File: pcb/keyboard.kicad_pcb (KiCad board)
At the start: 2 copper layers, 70 x 88.5 mm, 23 parts, among them SW1 SW_Push, SW2 SW_Push, SW3 RotaryEncoder_Switch, SW4 SW_Push, SW5 SW_Push, SW6 SW_Push, SW7 SW_Push, SW8 SW_Push, SW9 SW_Push, U1 MODULE-SEEEDUINO-XIAO-RP2040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

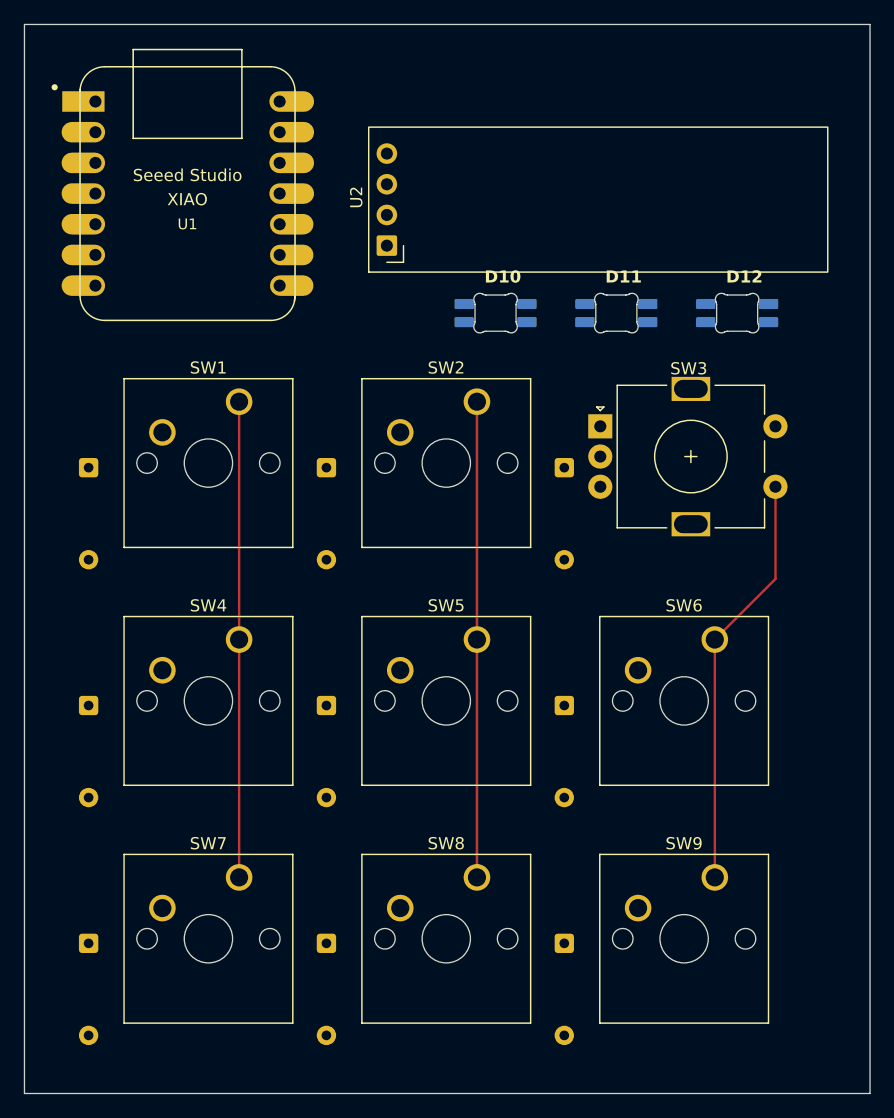
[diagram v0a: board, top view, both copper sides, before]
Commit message: align diodes in a better way
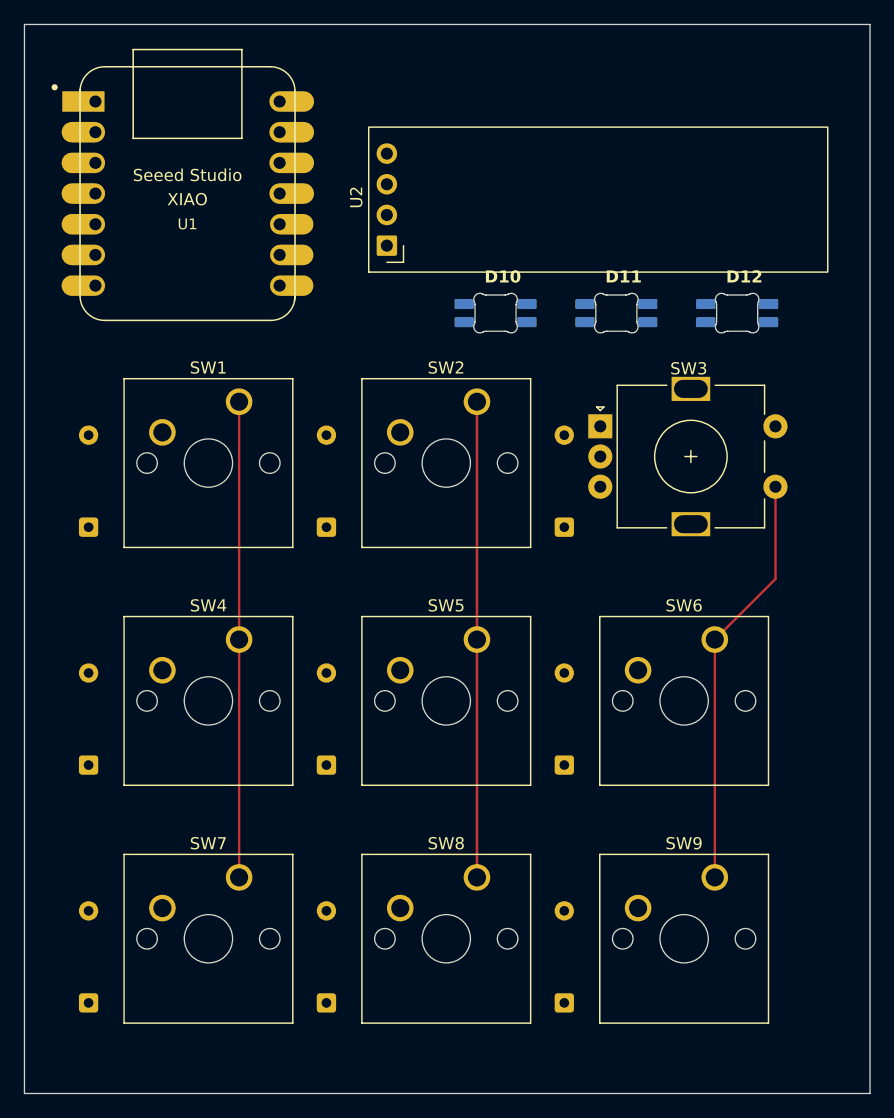
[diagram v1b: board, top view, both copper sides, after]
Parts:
- moved D1 59.3 mm to (205.2, 127.5), turned to 90 degrees
- moved D3 59.3 mm to (165.8, 127.5), turned to 90 degrees
- moved D7 52.3 mm to (205.2, 88.1), turned to 90 degrees
- moved D9 52.3 mm to (165.8, 88.1), turned to 90 degrees
- moved D2 44.3 mm to (185.5, 127.5), turned to 90 degrees
- moved D4 39.7 mm to (205.2, 107.8), turned to 90 degrees
- moved D6 39.7 mm to (165.8, 107.8), turned to 90 degrees
- moved D8 34.4 mm to (185.5, 88.1), turned to 90 degrees
- moved D5 4.93 mm to (185.5, 107.8), turned to 90 degrees

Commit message: align diodes correctly and connect them to the switches and in rows/columns
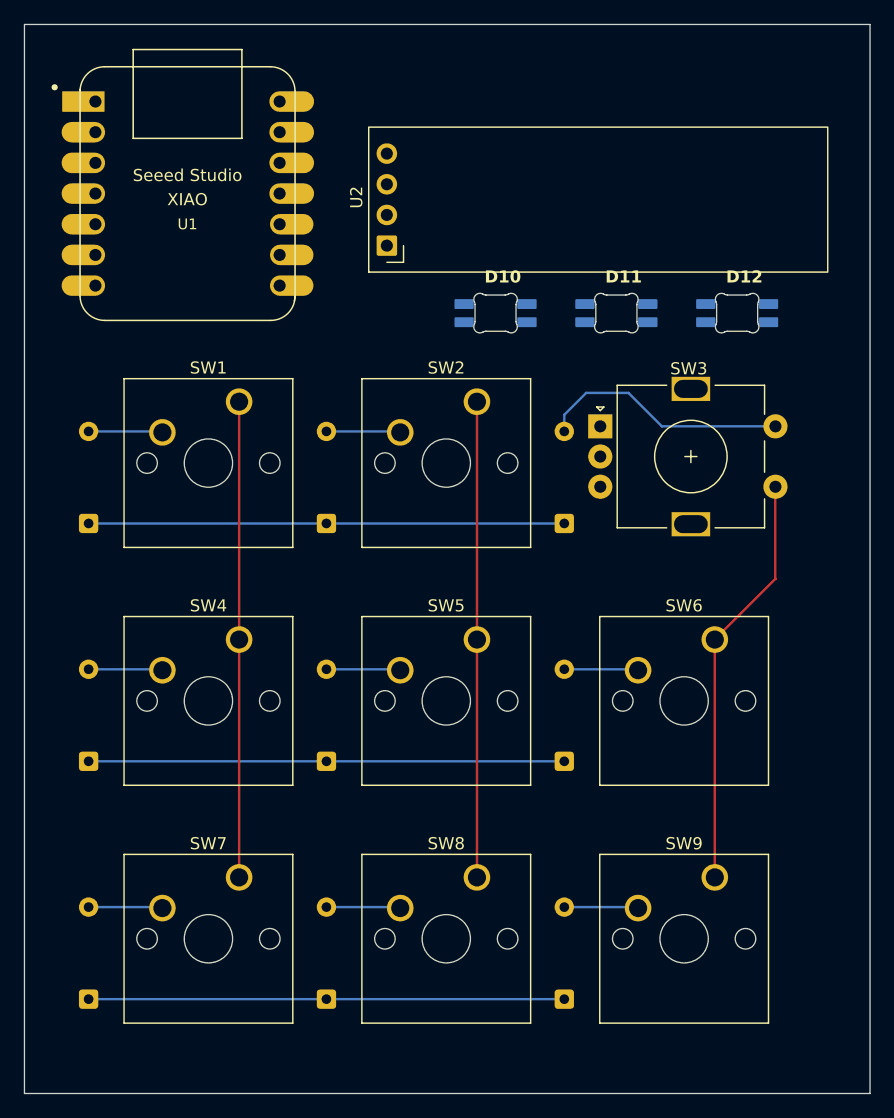
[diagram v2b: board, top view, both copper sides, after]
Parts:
- moved D1 55.9 mm to (165.8, 87.8)
- moved D3 55.9 mm to (205.2, 87.8)
- moved D7 55.5 mm to (165.8, 127.2)
- moved D9 55.5 mm to (205.2, 127.2)
- moved D2 39.7 mm to (185.5, 87.8)
- moved D4 39.4 mm to (165.8, 107.5)
- moved D6 39.4 mm to (205.2, 107.5)
- moved D8 39.1 mm to (185.5, 127.2)
- moved D5 0.31 mm to (185.5, 107.5)
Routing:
- net Row 2: track 0.00 -> 39.4 mm
- net Row 1: track 0.00 -> 39.4 mm
- net Row 0: track 0.00 -> 39.4 mm
- net ROT S2: track 0.00 -> 20.8 mm
- net Net-(D9-A): track 0.00 -> 6.14 mm
- net Net-(D8-A): track 0.00 -> 6.14 mm
- net Net-(D6-A): track 0.00 -> 6.14 mm
- net Net-(D5-A): track 0.00 -> 6.14 mm
- net Net-(D2-A): track 0.00 -> 6.14 mm
- net Net-(D7-A): track 0.00 -> 6.14 mm
- net Net-(D4-A): track 0.00 -> 6.14 mm
- net Net-(D1-A): track 0.00 -> 6.14 mm
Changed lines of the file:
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@@
 	(footprint "Diode_THT:D_DO-35_SOD27_P7.62mm_Horizontal"
 		(layer "B.Cu")
-		(at 185.5 127.5 90)
+		(at 185.5 87.81 90)
 		(descr "Diode, DO-35_SOD27 series, Axial, Horizontal, pin pitch=7.62mm, length*diameter=4*2mm^2, http://www.diodes.com/_files/packages/DO-35.pdf")
 		(tags "Diode DO-35_SOD27 series Axial Horizontal pin pitch 7.62mm  length 4mm diameter 2mm")
@@
 	(footprint "Diode_THT:D_DO-35_SOD27_P7.62mm_Horizontal"
 		(layer "B.Cu")
-		(at 205.19 88.12 90)
+		(at 165.81 127.19 90)
 		(descr "Diode, DO-35_SOD27 series, Axial, Horizontal, pin pitch=7.62mm, length*diameter=4*2mm^2, http://www.diodes.com/_files/packages/DO-35.pdf")
 		(tags "Diode DO-35_SOD27 series Axial Horizontal pin pitch 7.62mm  length 4mm diameter 2mm")
@@
 	(footprint "Diode_THT:D_DO-35_SOD27_P7.62mm_Horizontal"
 		(layer "B.Cu")
-		(at 185.5 88.12 90)
+		(at 185.5 127.19 90)
 		(descr "Diode, DO-35_SOD27 series, Axial, Horizontal, pin pitch=7.62mm, length*diameter=4*2mm^2, http://www.diodes.com/_files/packages/DO-35.pdf")
 		(tags "Diode DO-35_SOD27 series Axial Horizontal pin pitch 7.62mm  length 4mm diameter 2mm")
@@
 	(footprint "Diode_THT:D_DO-35_SOD27_P7.62mm_Horizontal"
 		(layer "B.Cu")
-		(at 165.81 127.5 90)
+		(at 205.19 87.81 90)
 		(descr "Diode, DO-35_SOD27 series, Axial, Horizontal, pin pitch=7.62mm, length*diameter=4*2mm^2, http://www.diodes.com/_files/packages/DO-35.pdf")
 		(tags "Diode DO-35_SOD27 series Axial Horizontal pin pitch 7.62mm  length 4mm diameter 2mm")
@@
 	(footprint "Diode_THT:D_DO-35_SOD27_P7.62mm_Horizontal"
 		(layer "B.Cu")
-		(at 165.81 107.81 90)
+		(at 205.19 107.5 90)
 		(descr "Diode, DO-35_SOD27 series, Axial, Horizontal, pin pitch=7.62mm, length*diameter=4*2mm^2, http://www.diodes.com/_files/packages/DO-35.pdf")
 		(tags "Diode DO-35_SOD27 series Axial Horizontal pin pitch 7.62mm  length 4mm diameter 2mm")
@@
 	(footprint "Diode_THT:D_DO-35_SOD27_P7.62mm_Horizontal"
 		(layer "B.Cu")
-		(at 205.19 107.81 90)
+		(at 165.81 107.5 90)
 		(descr "Diode, DO-35_SOD27 series, Axial, Horizontal, pin pitch=7.62mm, length*diameter=4*2mm^2, http://www.diodes.com/_files/packages/DO-35.pdf")
 		(tags "Diode DO-35_SOD27 series Axial Horizontal pin pitch 7.62mm  length 4mm diameter 2mm")
@@
 	(footprint "Diode_THT:D_DO-35_SOD27_P7.62mm_Horizontal"
 		(layer "B.Cu")
-		(at 185.5 107.81 90)
+		(at 185.5 107.5 90)
 		(descr "Diode, DO-35_SOD27 series, Axial, Horizontal, pin pitch=7.62mm, length*diameter=4*2mm^2, http://www.diodes.com/_files/packages/DO-35.pdf")
 		(tags "Diode DO-35_SOD27 series Axial Horizontal pin pitch 7.62mm  length 4mm diameter 2mm")
@@
 	(footprint "Diode_THT:D_DO-35_SOD27_P7.62mm_Horizontal"
 		(layer "B.Cu")
-		(at 165.81 88.12 90)
+		(at 205.19 127.19 90)
 		(descr "Diode, DO-35_SOD27 series, Axial, Horizontal, pin pitch=7.62mm, length*diameter=4*2mm^2, http://www.diodes.com/_files/packages/DO-35.pdf")
 		(tags "Diode DO-35_SOD27 series Axial Horizontal pin pitch 7.62mm  length 4mm diameter 2mm")
@@
 	(footprint "Diode_THT:D_DO-35_SOD27_P7.62mm_Horizontal"
 		(layer "B.Cu")
-		(at 205.19 127.5 90)
+		(at 165.81 87.81 90)
 		(descr "Diode, DO-35_SOD27 series, Axial, Horizontal, pin pitch=7.62mm, length*diameter=4*2mm^2, http://www.diodes.com/_files/packages/DO-35.pdf")
 		(tags "Diode DO-35_SOD27 series Axial Horizontal pin pitch 7.62mm  length 4mm diameter 2mm")
@@
 	)
 	(segment
+		(start 211.22 119.57)
+		(end 211.3 119.65)
+		(width 0.2)
+		(layer "B.Cu")
+		(net "Net-(D9-A)")
+	)
+	(segment
+		(start 205.19 119.57)
+		(end 211.22 119.57)
+		(width 0.2)
+		(layer "B.Cu")
+		(net "Net-(D9-A)")
+	)
+	(segment
 		(start 178.27 77.73)
 		(end 178.27 117.11)
@@
 		(net "Column 1")
 	)
+	(segment
+		(start 165.81 87.81)
+		(end 205.19 87.81)
+		(width 0.2)
+		(layer "B.Cu")
+		(net "Row 0")
+	)
+	(segment
+		(start 165.81 107.5)
+		(end 205.19 107.5)
+		(width 0.2)
+		(layer "B.Cu")
+		(net "Row 1")
+	)
+	(segment
+		(start 165.81 127.19)
+		(end 205.19 127.19)
+		(width 0.2)
+		(layer "B.Cu")
+		(net "Row 2")
+	)
+	(segment
+		(start 185.5 80.19)
+		(end 191.53 80.19)
+		(width 0.2)
+		(layer "B.Cu")
+		(net "Net-(D2-A)")
+	)
+	(segment
+		(start 191.53 80.19)
+		(end 191.61 80.27)
+		(width 0.2)
+		(layer "B.Cu")
+		(net "Net-(D2-A)")
+	)
+	(segment
+		(start 191.53 99.88)
+		(end 191.61 99.96)
+		(width 0.2)
+		(layer "B.Cu")
+		(net "Net-(D5-A)")
+	)
+	(segment
+		(start 185.5 99.88)
+		(end 191.53 99.88)
+		(width 0.2)
+		(layer "B.Cu")
+		(net "Net-(D5-A)")
+	)
+	(segment
+		(start 165.81 99.88)
+		(end 171.84 99.88)
+		(width 0.2)
+		(layer "B.Cu")
+		(net "Net-(D4-A)")
+	)
+	(segment
+		(start 171.84 99.88)
+		(end 171.92 99.96)
+		(width 0.2)
+		(layer "B.Cu")
+		(net "Net-(D4-A)")
+	)
+	(segment
+		(start 191.53 119.57)
+		(end 191.61 119.65)
+		(width 0.2)
+		(layer "B.Cu")
+		(net "Net-(D8-A)")
+	)
+	(segment
+		(start 185.5 119.57)
+		(end 191.53 119.57)
+		(width 0.2)
+		(layer "B.Cu")
+		(net "Net-(D8-A)")
+	)
+	(segment
+		(start 205.19 99.88)
+		(end 211.22 99.88)
+		(width 0.2)
+		(layer "B.Cu")
+		(net "Net-(D6-A)")
+	)
+	(segment
+		(start 211.22 99.88)
+		(end 211.3 99.96)
+		(width 0.2)
+		(layer "B.Cu")
+		(net "Net-(D6-A)")
+	)
+	(segment
+		(start 171.84 80.19)
+		(end 171.92 80.27)
+		(width 0.2)
+		(layer "B.Cu")
+		(net "Net-(D1-A)")
+	)
+	(segment
+		(start 165.81 80.19)
+		(end 171.84 80.19)
+		(width 0.2)
+		(layer "B.Cu")
+		(net "Net-(D1-A)")
+	)
+	(segment
+		(start 165.81 119.57)
+		(end 171.84 119.57)
+		(width 0.2)
+		(layer "B.Cu")
+		(net "Net-(D7-A)")
+	)
+	(segment
+		(start 171.84 119.57)
+		(end 171.92 119.65)
+		(width 0.2)
+		(layer "B.Cu")
+		(net "Net-(D7-A)")
+	)
+	(segment
+		(start 213.27 79.77)
+		(end 222.67 79.77)
+		(width 0.2)
+		(layer "B.Cu")
+		(net "ROT S2")
+	)
+	(segment
+		(start 205.19 78.81)
+		(end 207 77)
+		(width 0.2)
+		(layer "B.Cu")
+		(net "ROT S2")
+	)
+	(segment
+		(start 207 77)
+		(end 210.5 77)
+		(width 0.2)
+		(layer "B.Cu")
+		(net "ROT S2")
+	)
+	(segment
+		(start 210.5 77)
+		(end 213.27 79.77)
+		(width 0.2)
+		(layer "B.Cu")
+		(net "ROT S2")
+	)
+	(segment
+		(start 205.19 80.19)
+		(end 205.19 78.81)
+		(width 0.2)
+		(layer "B.Cu")
+		(net "ROT S2")
+	)
 	(embedded_fonts no)
